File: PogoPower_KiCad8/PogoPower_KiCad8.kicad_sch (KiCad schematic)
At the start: 6 parts, among them J1 Conn_01x01, J2 Conn_01x01, J3 Conn_01x01, J4 Conn_01x01, J5 Conn_01x01, J8 Conn_02x04_Odd_Even

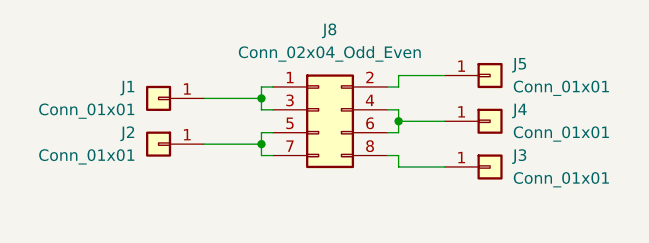
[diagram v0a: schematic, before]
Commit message: Pogo Power slikscreen
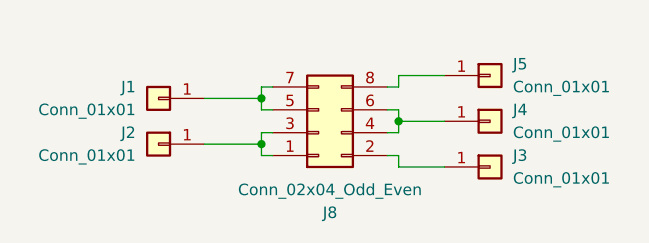
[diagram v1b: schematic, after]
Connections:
- net at J3.1 (Pin_1): now also J8.2 (Pin_2); no longer J8.8 (Pin_8)
- net at J5.1 (Pin_1): now also J8.8 (Pin_8); no longer J8.2 (Pin_2)
- net at J8.1 (Pin_1), J8.3 (Pin_3): now also J2.1 (Pin_1); no longer J1.1 (Pin_1)
- net at J8.5 (Pin_5), J8.7 (Pin_7): now also J1.1 (Pin_1); no longer J2.1 (Pin_1)
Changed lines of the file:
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@@
+	(wire
+		(pts
+			(xy 142.24 88.9) (xy 142.24 90.17)
+		)
+		(stroke
+			(width 0)
+			(type default)
+		)
+	)
+	(wire
+		(pts
+			(xy 157.48 97.79) (xy 162.56 97.79)
+		)
+		(stroke
+			(width 0)
+			(type default)
+		)
+	)
+	(wire
+		(pts
+			(xy 142.24 93.98) (xy 142.24 95.25)
+		)
+		(stroke
+			(width 0)
+			(type default)
+		)
+	)
+	(wire
+		(pts
+			(xy 156.21 96.52) (xy 157.48 96.52)
+		)
+		(stroke
+			(width 0)
+			(type default)
+		)
+	)
+	(wire
+		(pts
+			(xy 135.89 95.25) (xy 142.24 95.25)
+		)
+		(stroke
+			(width 0)
+			(type default)
+		)
+	)
+	(wire
+		(pts
+			(xy 157.48 92.71) (xy 162.56 92.71)
+		)
+		(stroke
+			(width 0)
+			(type default)
+		)
+	)
+	(wire
+		(pts
+			(xy 156.21 88.9) (xy 157.48 88.9)
+		)
+		(stroke
+			(width 0)
+			(type default)
+		)
+	)
+	(wire
+		(pts
+			(xy 156.21 91.44) (xy 157.48 91.44)
+		)
+		(stroke
+			(width 0)
+			(type default)
+		)
+	)
+	(wire
+		(pts
+			(xy 157.48 91.44) (xy 157.48 92.71)
+		)
+		(stroke
+			(width 0)
+			(type default)
+		)
+	)
+	(wire
+		(pts
+			(xy 156.21 93.98) (xy 157.48 93.98)
+		)
+		(stroke
+			(width 0)
+			(type default)
+		)
+	)
+	(wire
+		(pts
+			(xy 142.24 95.25) (xy 142.24 96.52)
+		)
+		(stroke
+			(width 0)
+			(type default)
+		)
+	)
+	(wire
+		(pts
+			(xy 135.89 90.17) (xy 142.24 90.17)
+		)
+		(stroke
+			(width 0)
+			(type default)
+		)
+	)
+	(wire
+		(pts
+			(xy 142.24 96.52) (xy 143.51 96.52)
+		)
+		(stroke
+			(width 0)
+			(type default)
+		)
+	)
+	(wire
+		(pts
+			(xy 157.48 88.9) (xy 157.48 87.63)
+		)
+		(stroke
+			(width 0)
+			(type default)
+		)
+	)
+	(wire
+		(pts
+			(xy 142.24 90.17) (xy 142.24 91.44)
+		)
+		(stroke
+			(width 0)
+			(type default)
+		)
+	)
+	(wire
+		(pts
+			(xy 157.48 96.52) (xy 157.48 97.79)
+		)
+		(stroke
+			(width 0)
+			(type default)
+		)
+	)
+	(wire
+		(pts
+			(xy 157.48 92.71) (xy 157.48 93.98)
+		)
+		(stroke
+			(width 0)
+			(type default)
+		)
+	)
+	(wire
+		(pts
+			(xy 142.24 93.98) (xy 143.51 93.98)
+		)
+		(stroke
+			(width 0)
+			(type default)
+		)
+	)
 	(wire
 		(pts
@@
 	(wire
 		(pts
-			(xy 142.24 88.9) (xy 142.24 90.17)
-		)
-		(stroke
-			(width 0)
-			(type default)
-		)
-	)
-	(wire
-		(pts
-			(xy 156.21 91.44) (xy 157.48 91.44)
-		)
-		(stroke
-			(width 0)
-			(type default)
-		)
-	)
-	(wire
-		(pts
-			(xy 157.48 97.79) (xy 162.56 97.79)
-		)
-		(stroke
-			(width 0)
-			(type default)
-		)
-	)
-	(wire
-		(pts
-			(xy 142.24 93.98) (xy 142.24 95.25)
-		)
-		(stroke
-			(width 0)
-			(type default)
-		)
-	)
-	(wire
-		(pts
-			(xy 156.21 96.52) (xy 157.48 96.52)
-		)
-		(stroke
-			(width 0)
-			(type default)
-		)
-	)
-	(wire
-		(pts
-			(xy 143.51 93.98) (xy 142.24 93.98)
-		)
-		(stroke
-			(width 0)
-			(type default)
-		)
-	)
-	(wire
-		(pts
-			(xy 135.89 95.25) (xy 142.24 95.25)
-		)
-		(stroke
-			(width 0)
-			(type default)
-		)
-	)
-	(wire
-		(pts
-			(xy 157.48 92.71) (xy 162.56 92.71)
-		)
-		(stroke
-			(width 0)
-			(type default)
-		)
-	)
-	(wire
-		(pts
-			(xy 143.51 88.9) (xy 142.24 88.9)
-		)
-		(stroke
-			(width 0)
-			(type default)
-		)
-	)
-	(wire
-		(pts
-			(xy 157.48 91.44) (xy 157.48 92.71)
-		)
-		(stroke
-			(width 0)
-			(type default)
-		)
-	)
-	(wire
-		(pts
-			(xy 142.24 95.25) (xy 142.24 96.52)
-		)
-		(stroke
-			(width 0)
-			(type default)
-		)
-	)
-	(wire
-		(pts
-			(xy 135.89 90.17) (xy 142.24 90.17)
-		)
-		(stroke
-			(width 0)
-			(type default)
-		)
-	)
-	(wire
-		(pts
-			(xy 157.48 88.9) (xy 157.48 87.63)
-		)
-		(stroke
-			(width 0)
-			(type default)
-		)
-	)
-	(wire
-		(pts
-			(xy 142.24 90.17) (xy 142.24 91.44)
-		)
-		(stroke
-			(width 0)
-			(type default)
-		)
-	)
-	(wire
-		(pts
-			(xy 157.48 96.52) (xy 157.48 97.79)
-		)
-		(stroke
-			(width 0)
-			(type default)
-		)
-	)
-	(wire
-		(pts
-			(xy 156.21 88.9) (xy 157.48 88.9)
-		)
-		(stroke
-			(width 0)
-			(type default)
-		)
-	)
-	(wire
-		(pts
-			(xy 157.48 92.71) (xy 157.48 93.98)
-		)
-		(stroke
-			(width 0)
-			(type default)
-		)
-	)
-	(wire
-		(pts
-			(xy 157.48 93.98) (xy 156.21 93.98)
-		)
-		(stroke
-			(width 0)
-			(type default)
-		)
-	)
-	(wire
-		(pts
-			(xy 142.24 96.52) (xy 143.51 96.52)
-		)
-		(stroke
-			(width 0)
-			(type default)
-		)
-	)
-	(wire
-		(pts
 			(xy 157.48 87.63) (xy 162.56 87.63)
+		)
+		(stroke
+			(width 0)
+			(type default)
+		)
+	)
+	(wire
+		(pts
+			(xy 142.24 88.9) (xy 143.51 88.9)
 		)
 		(stroke
@@
 	(symbol
 		(lib_id "Connector_Generic:Conn_02x04_Odd_Even")
-		(at 148.59 91.44 0)
+		(at 148.59 93.98 0)
+		(mirror x)
 		(unit 1)
 		(exclude_from_sim no)
@@
 		(on_board yes)
 		(dnp no)
-		(fields_autoplaced yes)
 		(property "Reference" "J8"
-			(at 149.86 82.55 0)
+			(at 149.86 102.87 0)
 			(effects
 				(font
@@
 		)
 		(property "Value" "Conn_02x04_Odd_Even"
-			(at 149.86 85.09 0)
+			(at 149.86 100.33 0)
 			(effects
 				(font
@@
 		)
 		(property "Footprint" "Connector_PinHeader_2.54mm:PinHeader_2x04_P2.54mm_Vertical"
-			(at 148.59 91.44 0)
+			(at 148.59 93.98 0)
 			(effects
 				(font
@@
 		)
 		(property "Datasheet" "~"
-			(at 148.59 91.44 0)
+			(at 148.59 93.98 0)
 			(effects
 				(font
@@
 		)
 		(property "Description" "Generic connector, double row, 02x04, odd/even pin numbering scheme (row 1 odd numbers, row 2 even numbers), script generated (kicad-library-utils/schlib/autogen/connector/)"
-			(at 148.59 91.44 0)
-			(effects
-				(font
+			(at 148.59 93.98 0)
+			(effects
+				(font
